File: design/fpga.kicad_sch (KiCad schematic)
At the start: 80 parts, among them J7 DEBUG_FPGA_GPIO, J8 DIGILENT_JTAG_HS2_01X06, SW1 RST, SW2 PROG, U13 XC7S15-FTGB196, U14 IS25LP064A-JKx

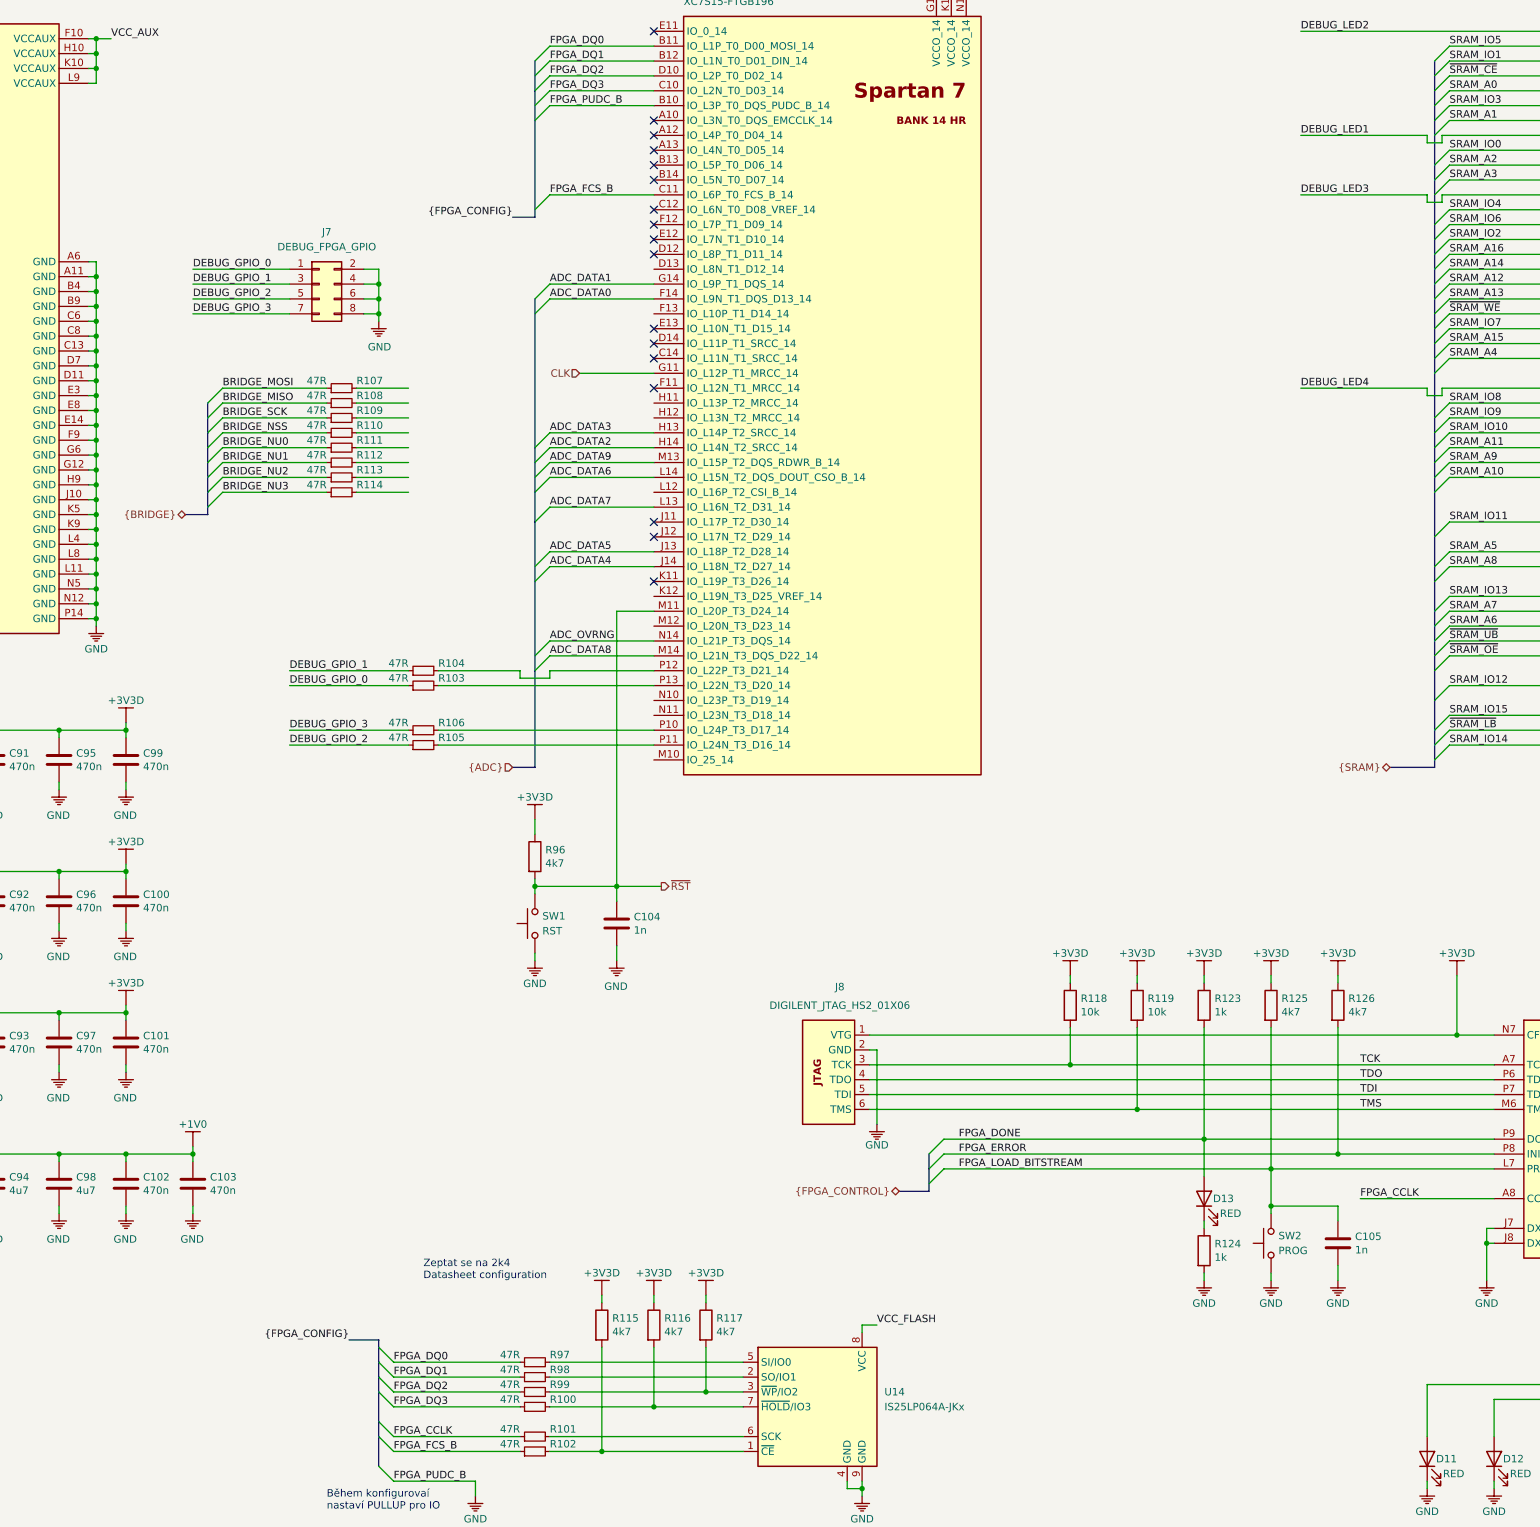
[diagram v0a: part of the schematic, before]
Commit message: Added SPI connection
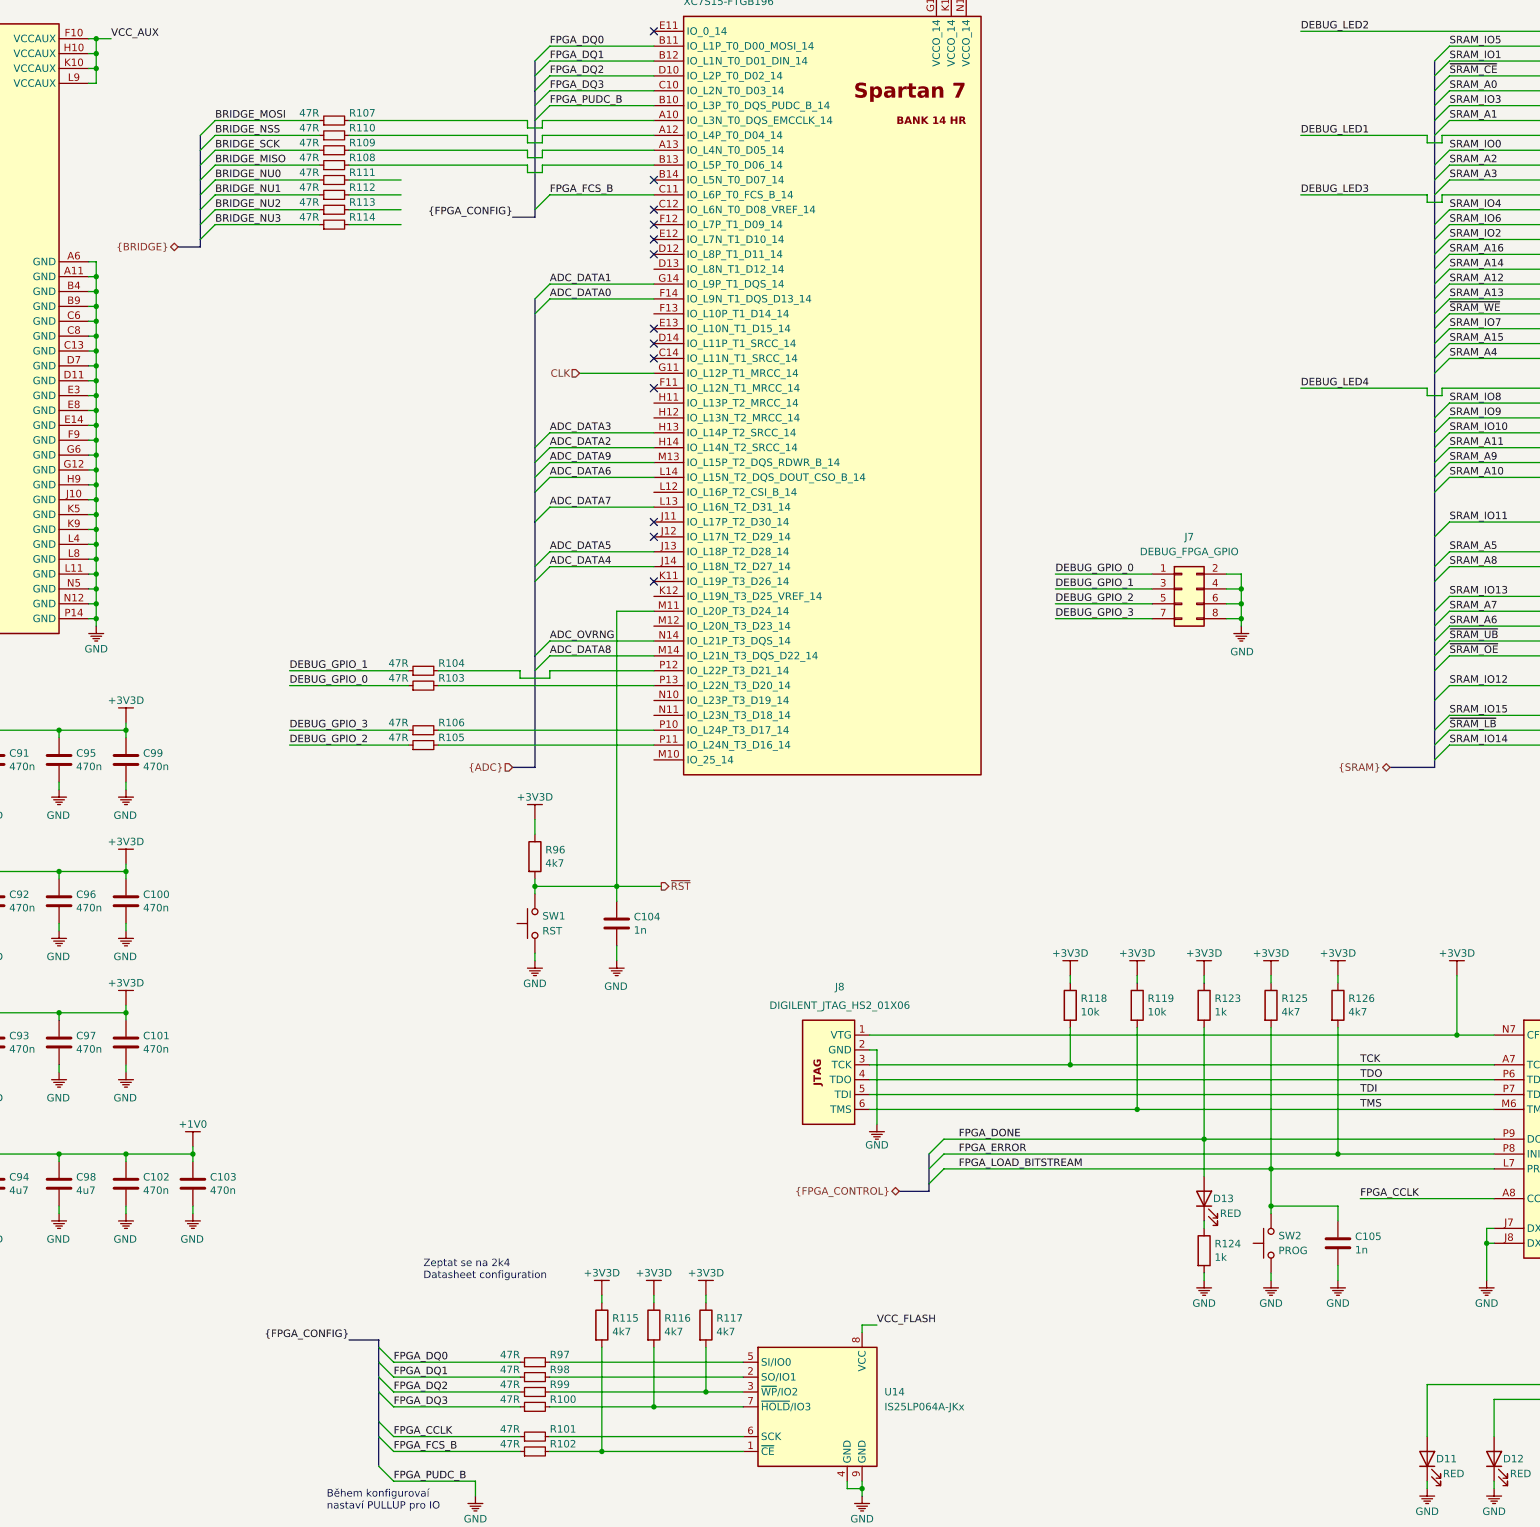
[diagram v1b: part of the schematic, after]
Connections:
- net at R107.2: now also U13.A10 (IO_L3N_T0_DQS_EMCCLK_14)
- net at U13.A12 (IO_L4P_T0_D04_14): now also R110.2
- net at U13.A13 (IO_L4N_T0_D05_14): now also R109.2
- net at U13.B13 (IO_L5P_T0_D06_14): now also R108.2
- no-connect marks 25 -> 21
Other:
- moved on the sheet: J7, R107, R108, R109, R110, R111, R112, R113, R114

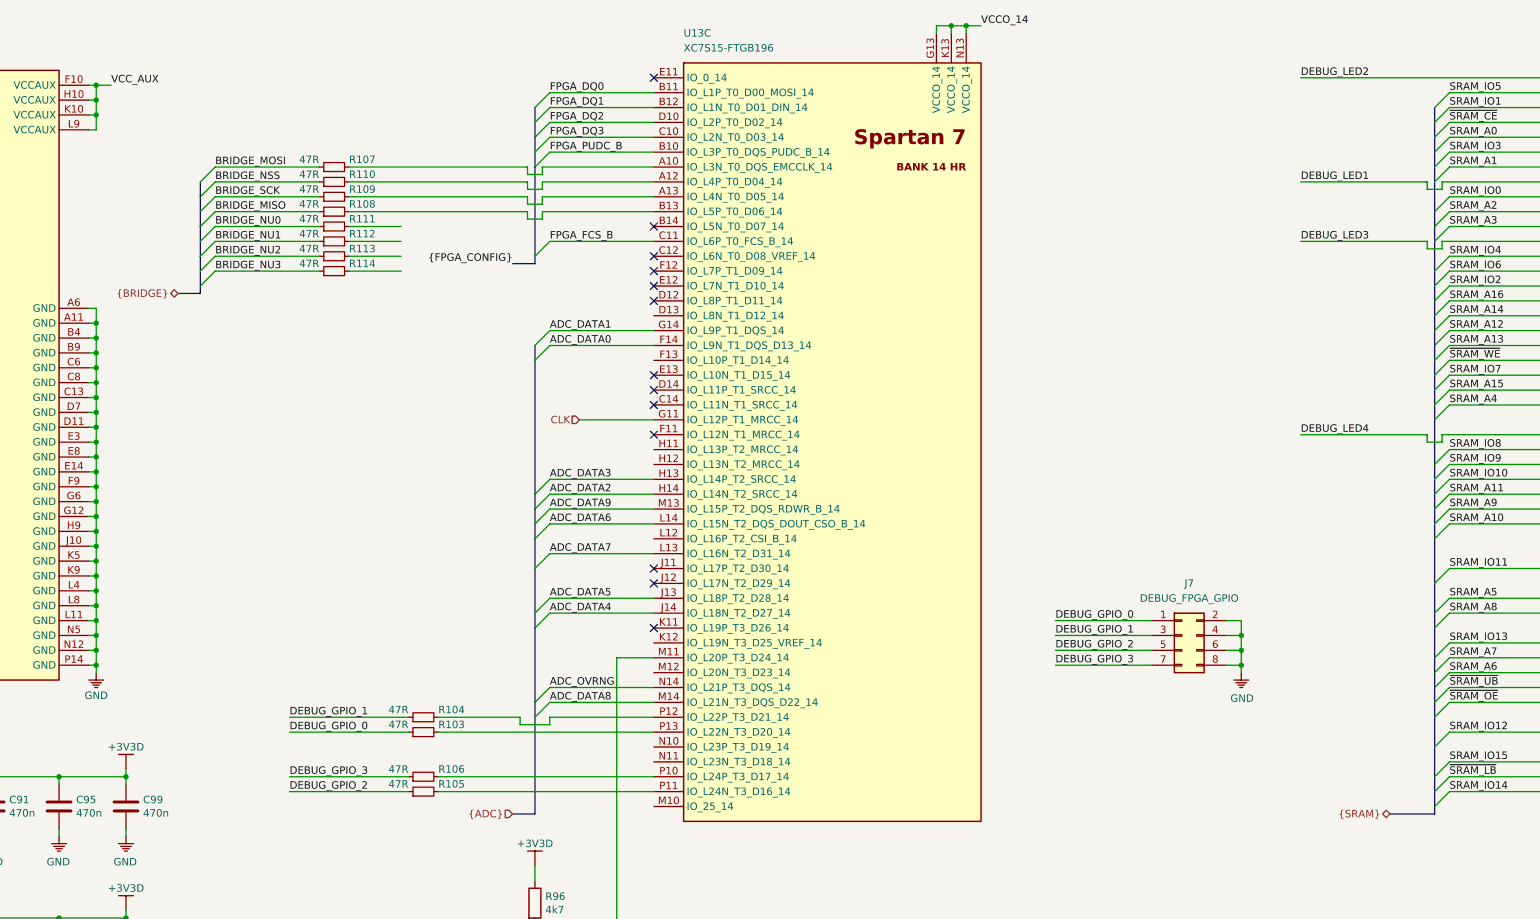
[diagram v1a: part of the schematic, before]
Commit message: Added bridge connection
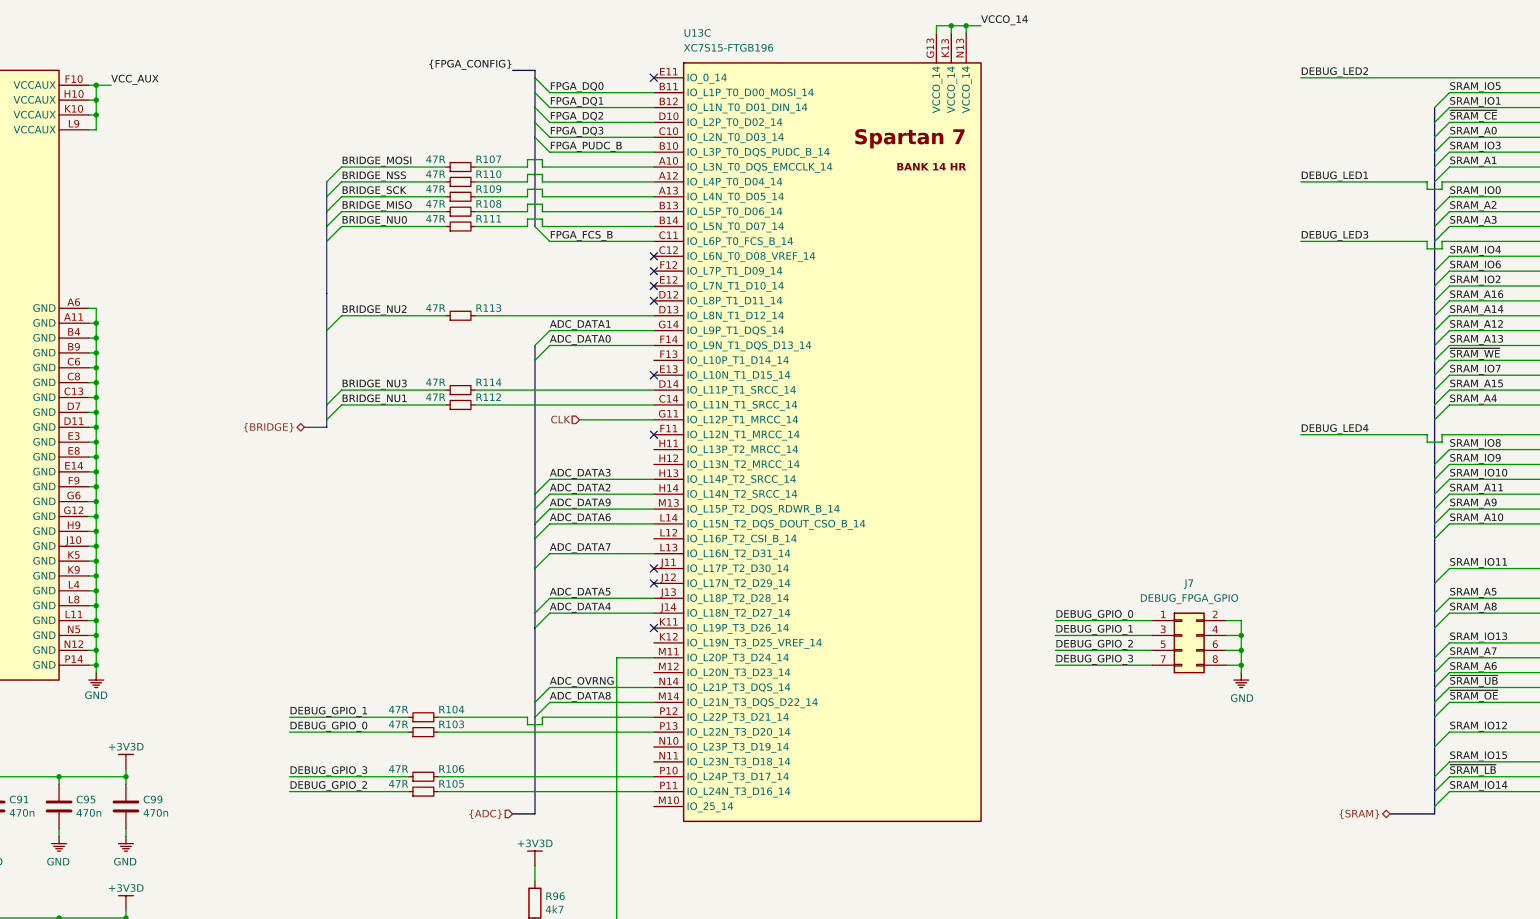
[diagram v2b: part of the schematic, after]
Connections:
- net at R111.2: now also U13.B14 (IO_L5N_T0_D07_14)
- net at U13.C14 (IO_L11N_T1_SRCC_14): now also R112.2
- net at U13.D13 (IO_L8N_T1_D12_14): now also R113.2
- net at U13.D14 (IO_L11P_T1_SRCC_14): now also R114.2
- no-connect marks 21 -> 18
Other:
- moved on the sheet: R107, R108, R109, R110, R111, R112, R113, R114

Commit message: Small layout update
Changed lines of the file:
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@@
   (bus (pts (xy 125.73 85.09) (xy 129.54 85.09)))
   (bus (pts (xy 129.54 43.18) (xy 129.54 48.26)))
-  (bus (pts (xy 129.54 48.26) (xy 129.54 50.8)))
-  (bus (pts (xy 129.54 50.8) (xy 129.54 62.23)))
+  (bus (pts (xy 129.54 48.26) (xy 129.54 53.34)))
+  (bus (pts (xy 129.54 53.34) (xy 129.54 62.23)))
   (bus (pts (xy 129.54 62.23) (xy 129.54 81.28)))
   (bus (pts (xy 129.54 81.28) (xy 129.54 85.09)))
@@
   (bus (pts (xy 165.1 35.56) (xy 165.1 50.8)))
   (bus (pts (xy 165.1 71.12) (xy 165.1 96.52)))
-  (bus (pts (xy 165.1 96.52) (xy 165.1 101.6)))
-  (bus (pts (xy 165.1 101.6) (xy 165.1 109.22)))
-  (bus (pts (xy 165.1 109.22) (xy 165.1 119.38)))
+  (bus (pts (xy 165.1 96.52) (xy 165.1 99.06)))
+  (bus (pts (xy 165.1 99.06) (xy 165.1 104.14)))
+  (bus (pts (xy 165.1 104.14) (xy 165.1 116.84)))
+  (bus (pts (xy 165.1 116.84) (xy 165.1 119.38)))
   (bus (pts (xy 165.1 119.38) (xy 165.1 134.62)))
   (bus (pts (xy 165.1 134.62) (xy 165.1 151.13)))
